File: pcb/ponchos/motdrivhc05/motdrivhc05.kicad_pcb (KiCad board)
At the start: 2 copper layers, 55.2 x 69.5 mm, 22 parts, among them J1 Screw_Terminal_1x06, J3 GW-040, U1 L293

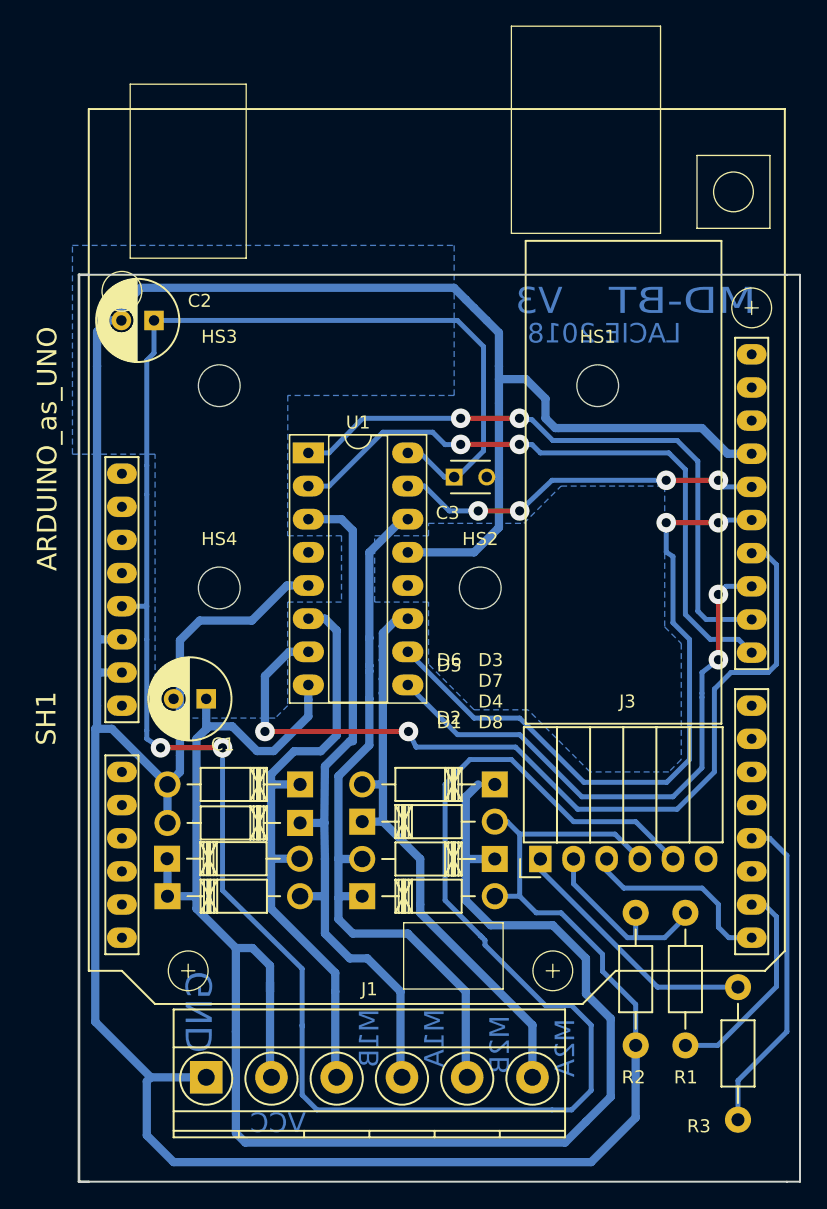
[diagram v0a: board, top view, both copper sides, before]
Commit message: Ensancho vías y agujeros.
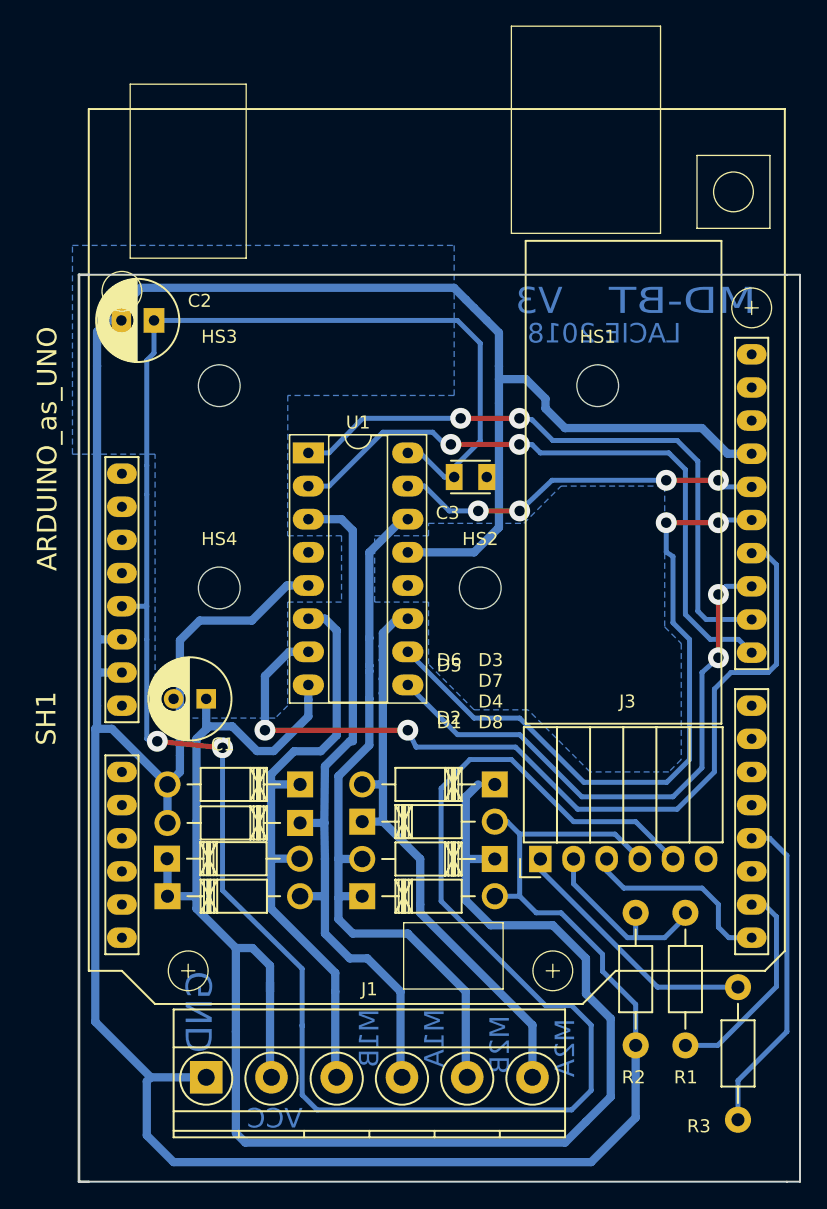
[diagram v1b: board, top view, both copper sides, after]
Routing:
- net GND: track 267.0 -> 266.4 mm

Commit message: Correción del demo original de control de motores. Correción en PBC.
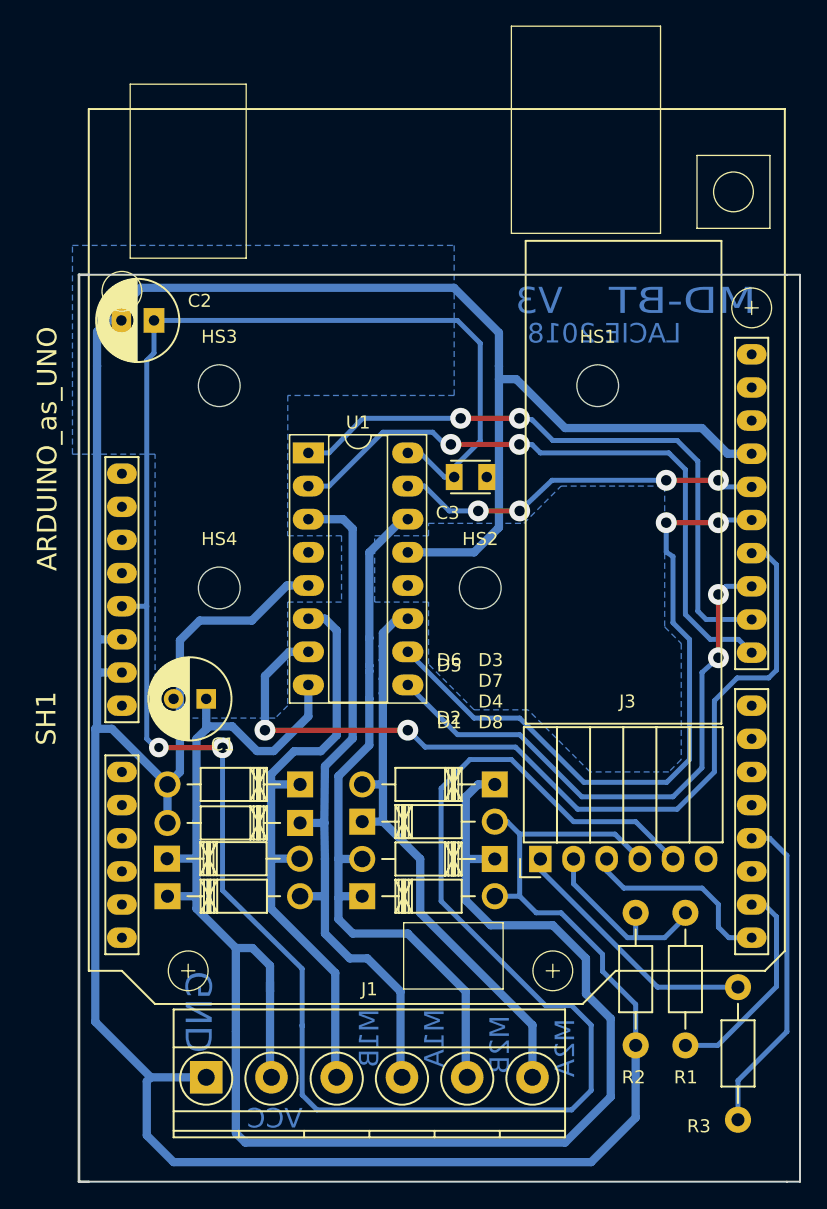
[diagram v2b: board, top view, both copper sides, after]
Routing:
- net VCC: track 130.9 -> 130.3 mm
- net /2A: track 69.1 -> 68.6 mm

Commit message: motdrivhc05: -Migración a Kicad 5. -Eliminación de varios puentes, algunos que podían hacer contacto con el módulo bluetooth. -Vinculado pin Vin de Arduino con linea de VCC. -Bloques de terminales en grupos de 2 conexiones separados. -Cambio de footprints de diodos.
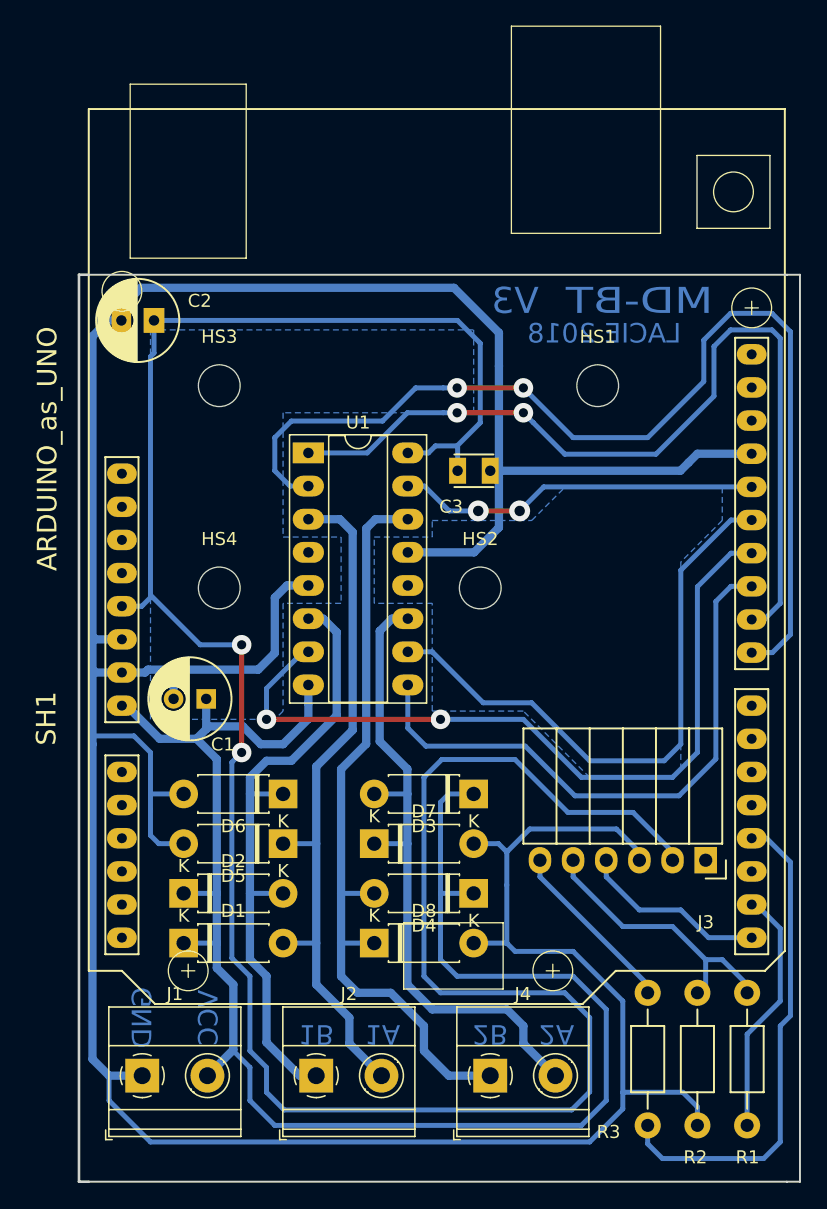
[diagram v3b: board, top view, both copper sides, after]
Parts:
- added J2: Screw_Terminal_01x02, TerminalBlock_Phoenix:TerminalBlock_Phoenix_MKDS-1,5-2_1x02_P5.00mm_Horizontal, F.Cu at (43.5, 80.0)
- added J4: Screw_Terminal_01x02, TerminalBlock_Phoenix:TerminalBlock_Phoenix_MKDS-1,5-2_1x02_P5.00mm_Horizontal, F.Cu at (56.8, 80.0)
- D1, D2, D3, D4, D5, D6, D7, D8: footprint Diodes_ThroughHole:Diode_DO-41_SOD81_Horizontal_RM10 -> Diode_THT:D_DO-41_SOD81_P7.62mm_Horizontal
- J1: value Screw_Terminal_1x06 -> Screw_Terminal_01x02; footprint Terminal_Blocks:TerminalBlock_Pheonix_MKDS1.5-6pol -> TerminalBlock_Phoenix:TerminalBlock_Phoenix_MKDS-1,5-2_1x02_P5.00mm_Horizontal
- moved J3 12.7 mm to (73.3, 63.5)
- moved R1 7.74 mm to (76.5, 83.8)
- moved R2 7.74 mm to (72.7, 73.7)
- moved R3 6.93 mm to (68.9, 83.8)
- moved J1 4.91 mm to (30.2, 80.0)
- moved D1 3.80 mm to (33.3, 69.8)
- moved D8 3.71 mm to (47.9, 69.8)
- moved D4 3.10 mm to (55.6, 66.0)
- moved D2 2.94 mm to (33.3, 66.0)
- moved D5 2.06 mm to (41.0, 62.2)
- moved D7 1.92 mm to (47.9, 62.2)
- moved D3 1.78 mm to (55.6, 58.4)
- moved D6 1.49 mm to (41.0, 58.4)
- moved C3 0.55 mm to (54.3, 33.7)
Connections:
- J3 pad 2: Net-(J3-Pad2) -> +5V
- J3 pad 3: /BT_TXD -> GND
- J3 pad 4: GND -> /BT_TXD
- J3 pad 5: +5V -> Net-(J3-Pad5)
- R1 pad 2: Net-(J3-Pad2) -> Net-(J3-Pad5)
- R2 pad 1: Net-(J3-Pad2) -> Net-(J3-Pad5)
- R3 pad 2: Net-(J3-Pad1) -> Net-(J3-Pad6)
- SH1 pad VIN: Net-(SH1-PadVIN) -> VCC
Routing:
- net /1A: track 49.2 -> 81.4 mm
- net Net-(J3-Pad5): track 0.00 -> 21.5 mm
- net /ME12: track 48.2 -> 68.2 mm
- net Net-(J3-Pad1): track 19.7 -> 0.00 mm
- net Net-(J3-Pad2): track 15.4 -> 0.00 mm
- net Net-(J3-Pad6): track 0.00 -> 13.8 mm
- net /BT_STATE: track 25.1 -> 38.1 mm
- net GND: track 266.0 -> 275.8 mm
- net /2A: track 68.6 -> 61.0 mm
- net +5V: track 185.9 -> 193.0 mm
- net /3A: track 52.4 -> 45.6 mm, vias 2 -> 0
- net /M2A: track 45.2 -> 51.3 mm
- net /M2B: track 55.5 -> 59.4 mm
- net VCC: track 130.3 -> 127.2 mm
- net /BT_RXD: track 16.5 -> 19.1 mm
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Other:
- board text added: "1A"
- board text added: "1B"
- board text added: "2A"
- board text added: "2B"
- board text removed: "M1A"
- board text removed: "M1B"
- board text removed: "M2A"
- board text removed: "M2B"

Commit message: motdrivhc05: -Correción en la especificación de orificios.
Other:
- board text added: "Taladros: J1, J2, J4 -> 1.25mm J3, SH1, D1-D9, -> 0.9mm Todos los demas -> 0.7mm"
- board text removed: "Taladros: J1 -> 1.25mm J3, J4, SH1, D1-D9, Q1 -> 0.9mm Todos los demas -> 0.7mm"
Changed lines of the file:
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@@
     (effects (font (size 1.5 1.5) (thickness 0.25)) (justify mirror))
   )
-  (gr_text "Taladros:\n\nJ1 -> 1.25mm\nJ3, J4, SH1, D1-D9, Q1 -> 0.9mm\nTodos los demas -> 0.7mm" (at 102.5525 41.91) (layer Dwgs.User)
+  (gr_text "Taladros:\n\nJ1, J2, J4 -> 1.25mm\nJ3, SH1, D1-D9,  -> 0.9mm\nTodos los demas -> 0.7mm" (at 102.5525 41.91) (layer Dwgs.User)
     (effects (font (size 1.5 1.5) (thickness 0.3)) (justify left))
   )
